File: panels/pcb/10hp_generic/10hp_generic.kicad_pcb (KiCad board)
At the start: 2 copper layers, 48.8 x 106 mm, 89 parts, among them J1 CAN_PWR, J2 SWD, J3 I2C, SW1 SW_Push, SW10 SW_Push, SW11 SW_Push, SW12 SW_Push, SW13 SW_Push, SW14 SW_Push, SW15 SW_Push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

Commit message: Updated PCB fixing issues with r3:   Reversed power pins on U1.   Increase size of potentiometer anchors holes. Enable external high speed clock. Enable all LEDs, switches and pots.
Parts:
- turned C40 to -90 degrees
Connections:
- U1 pad 2: +5V -> GND
- U1 pad 3: GND -> +5V
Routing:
- net GND: track 630.1 -> 636.0 mm
- net +5V: track 462.9 -> 464.5 mm

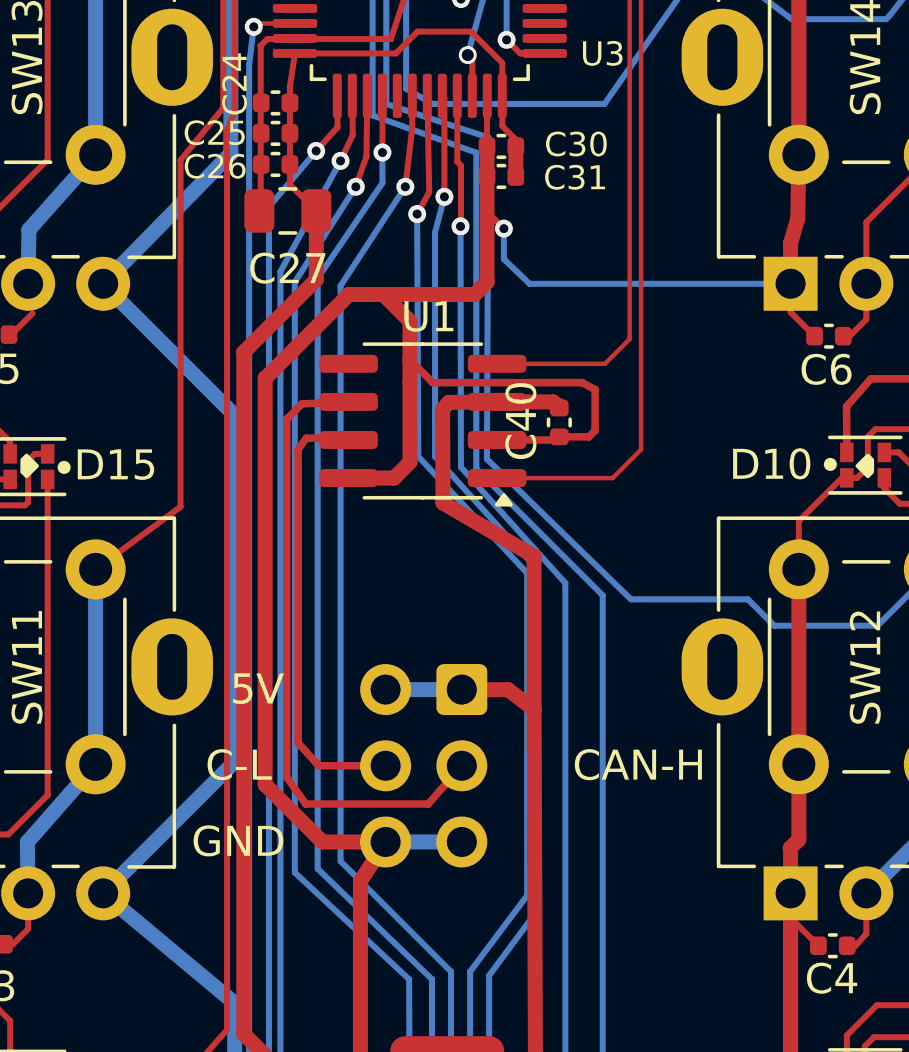
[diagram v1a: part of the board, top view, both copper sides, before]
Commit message: Fixes to generic 10hp schematic and PCB
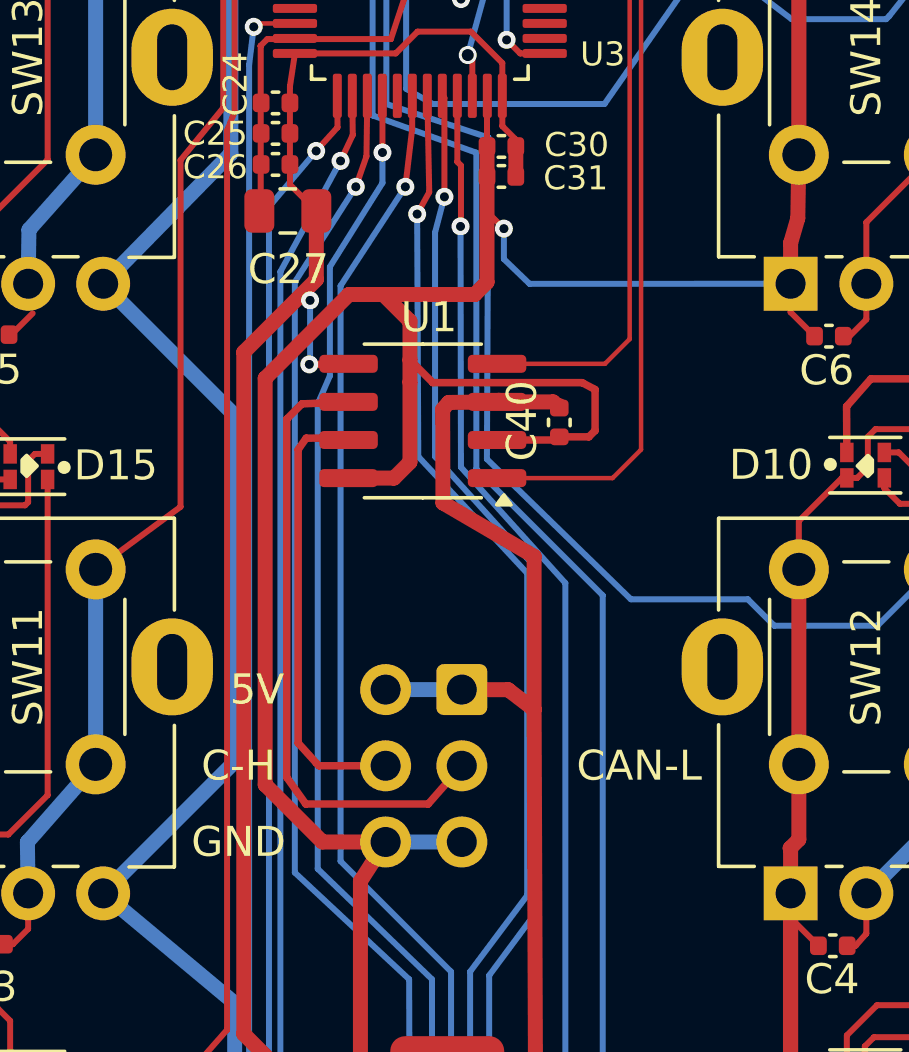
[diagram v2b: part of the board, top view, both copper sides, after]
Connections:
- J1 pad 3: CAN-H -> CAN-L
- J1 pad 4: CAN-L -> CAN-H
- U1 pad 5: unconnected-(U1-VIO-Pad5) -> VDD
- U1 pad 6: CAN-H -> CAN-L
- U1 pad 7: CAN-L -> CAN-H
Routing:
- net CAN-L: track 15.0 -> 21.1 mm
- net CAN-H: track 21.1 -> 15.0 mm
- net VDD: track 356.4 -> 360.7 mm, vias 0 -> 2
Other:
- board text added: "C-H"
- board text removed: "C-L"
